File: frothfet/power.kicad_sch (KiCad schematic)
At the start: 41 parts, among them J1 Screw_Terminal_01x08, J2 Screw_Terminal_01x08, U27 TPS7A2033PDBVR, U28 MCP3425A0T-ECH, U30 XL1509-5.0

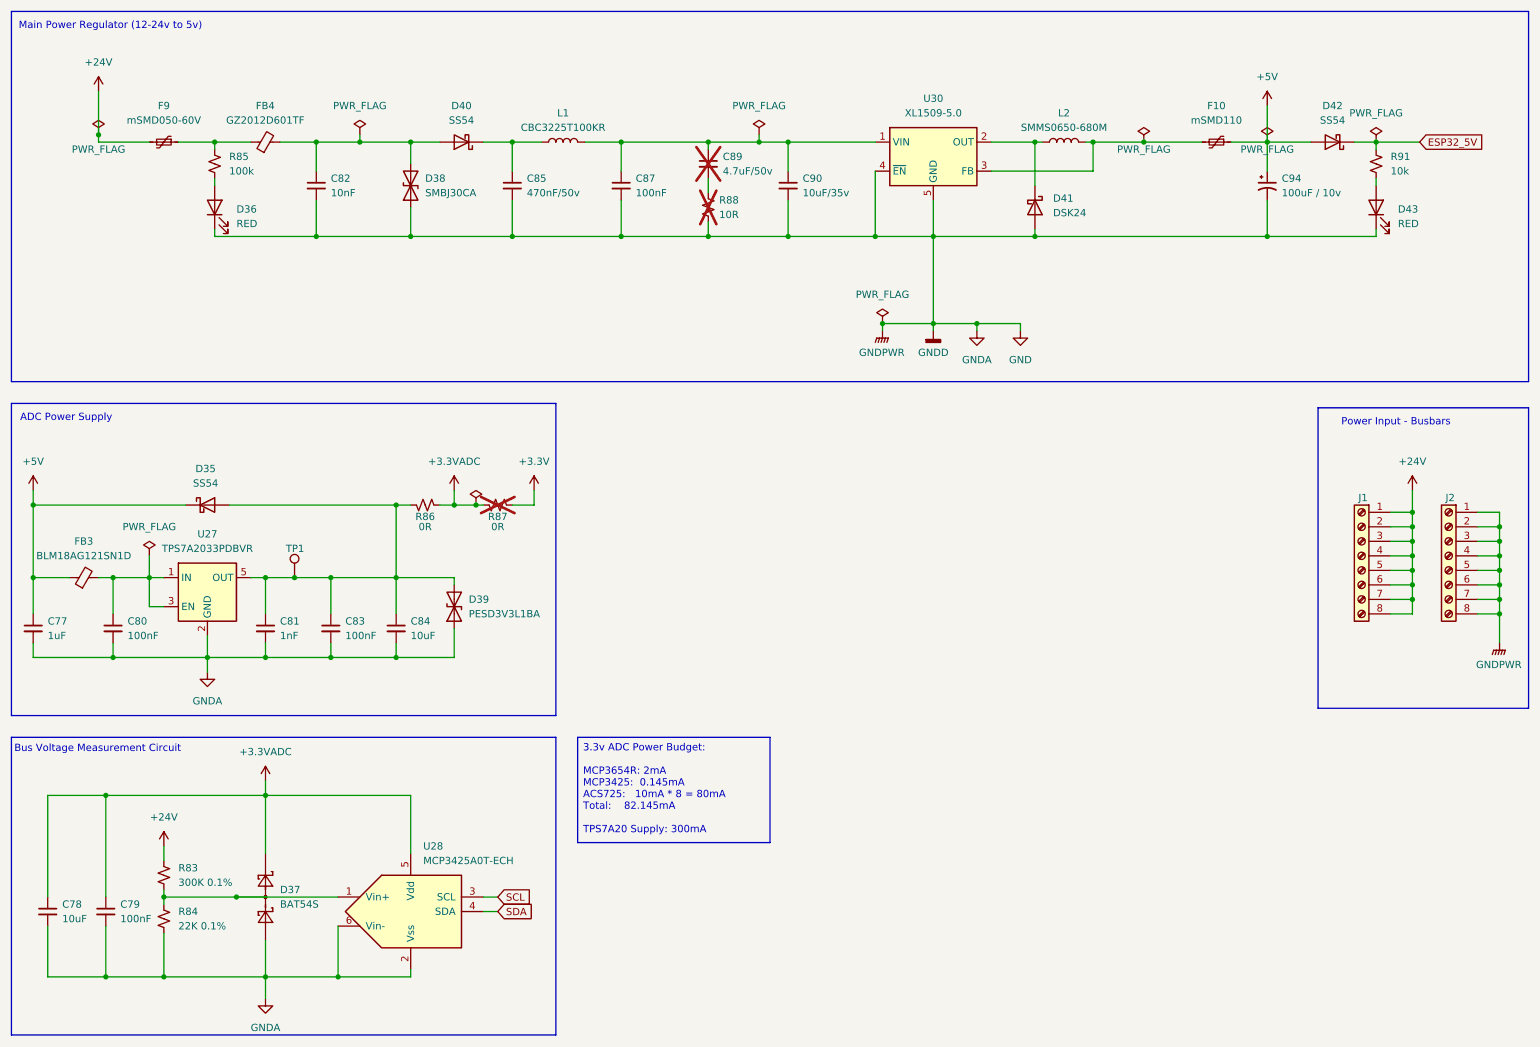
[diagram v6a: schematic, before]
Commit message: wired the i2c addresses.
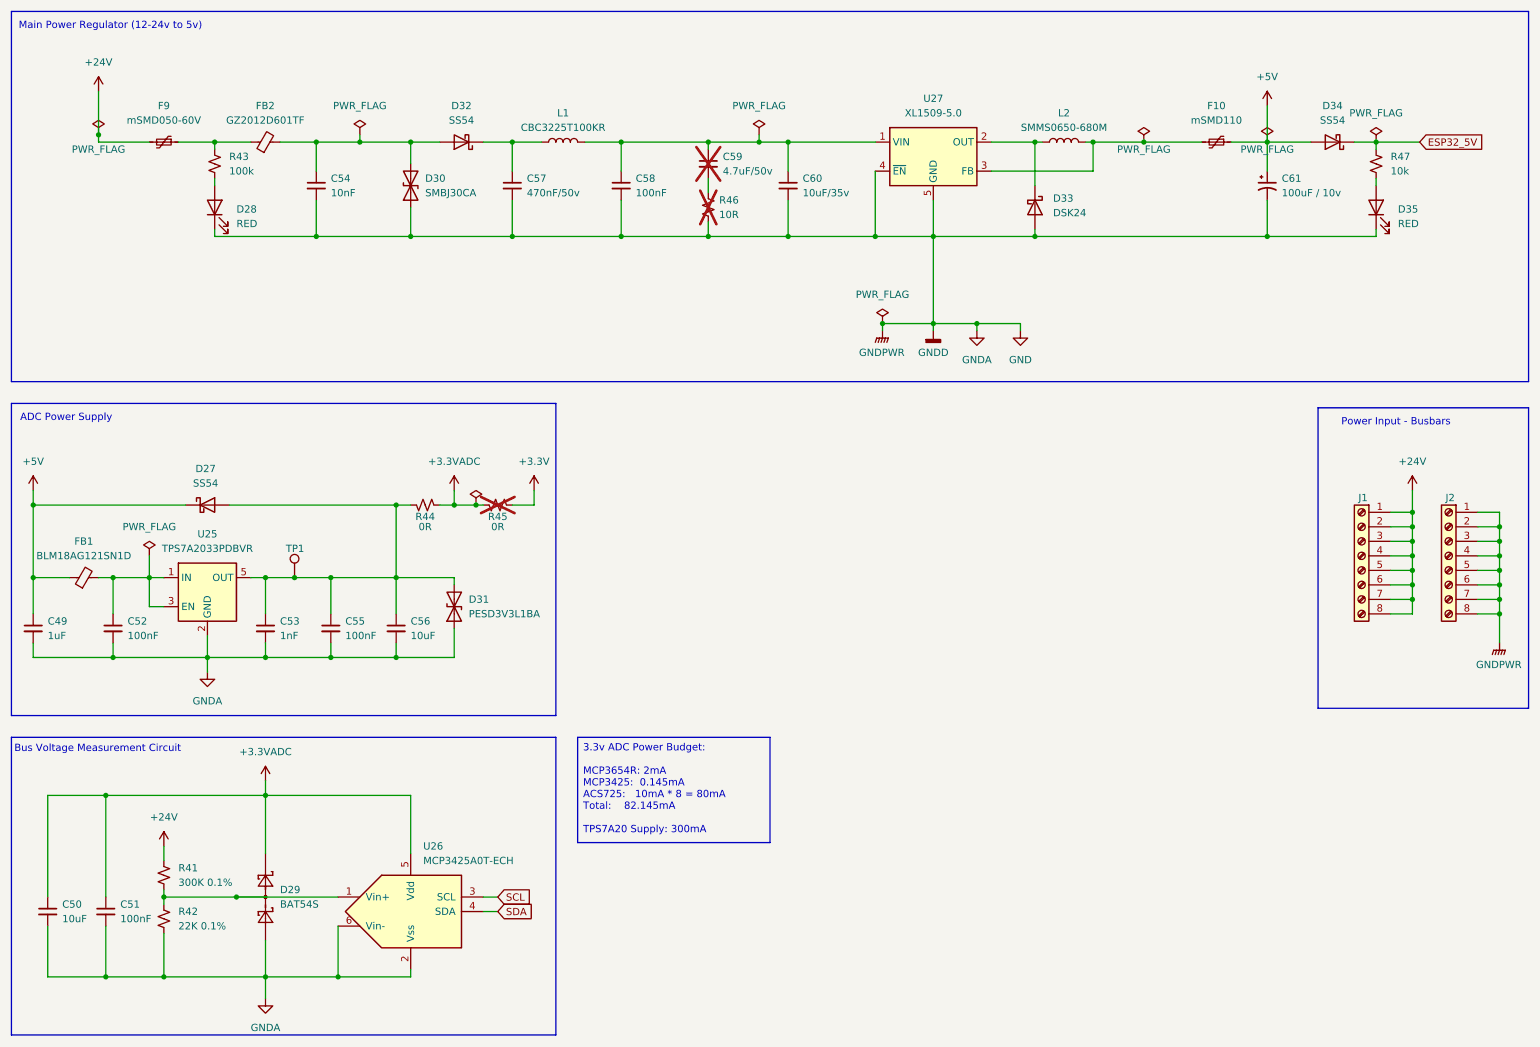
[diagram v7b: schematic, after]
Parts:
- renumbered C77 to C49, C78 to C50, C79 to C51, C80 to C52, C81 to C53, C82 to C54, C83 to C55, C84 to C56, C85 to C57, C87 to C58, C89 to C59, C90 to C60, C94 to C61, D35 to D27, D36 to D28, D37 to D29, D38 to D30, D39 to D31, D40 to D32, D41 to D33, D42 to D34, D43 to D35, FB3 to FB1, FB4 to FB2, R83 to R41, R84 to R42, R85 to R43, R86 to R44, R87 to R45, R88 to R46, R91 to R47, U27 to U25, U28 to U26, U30 to U27

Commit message: added the buffer circuit
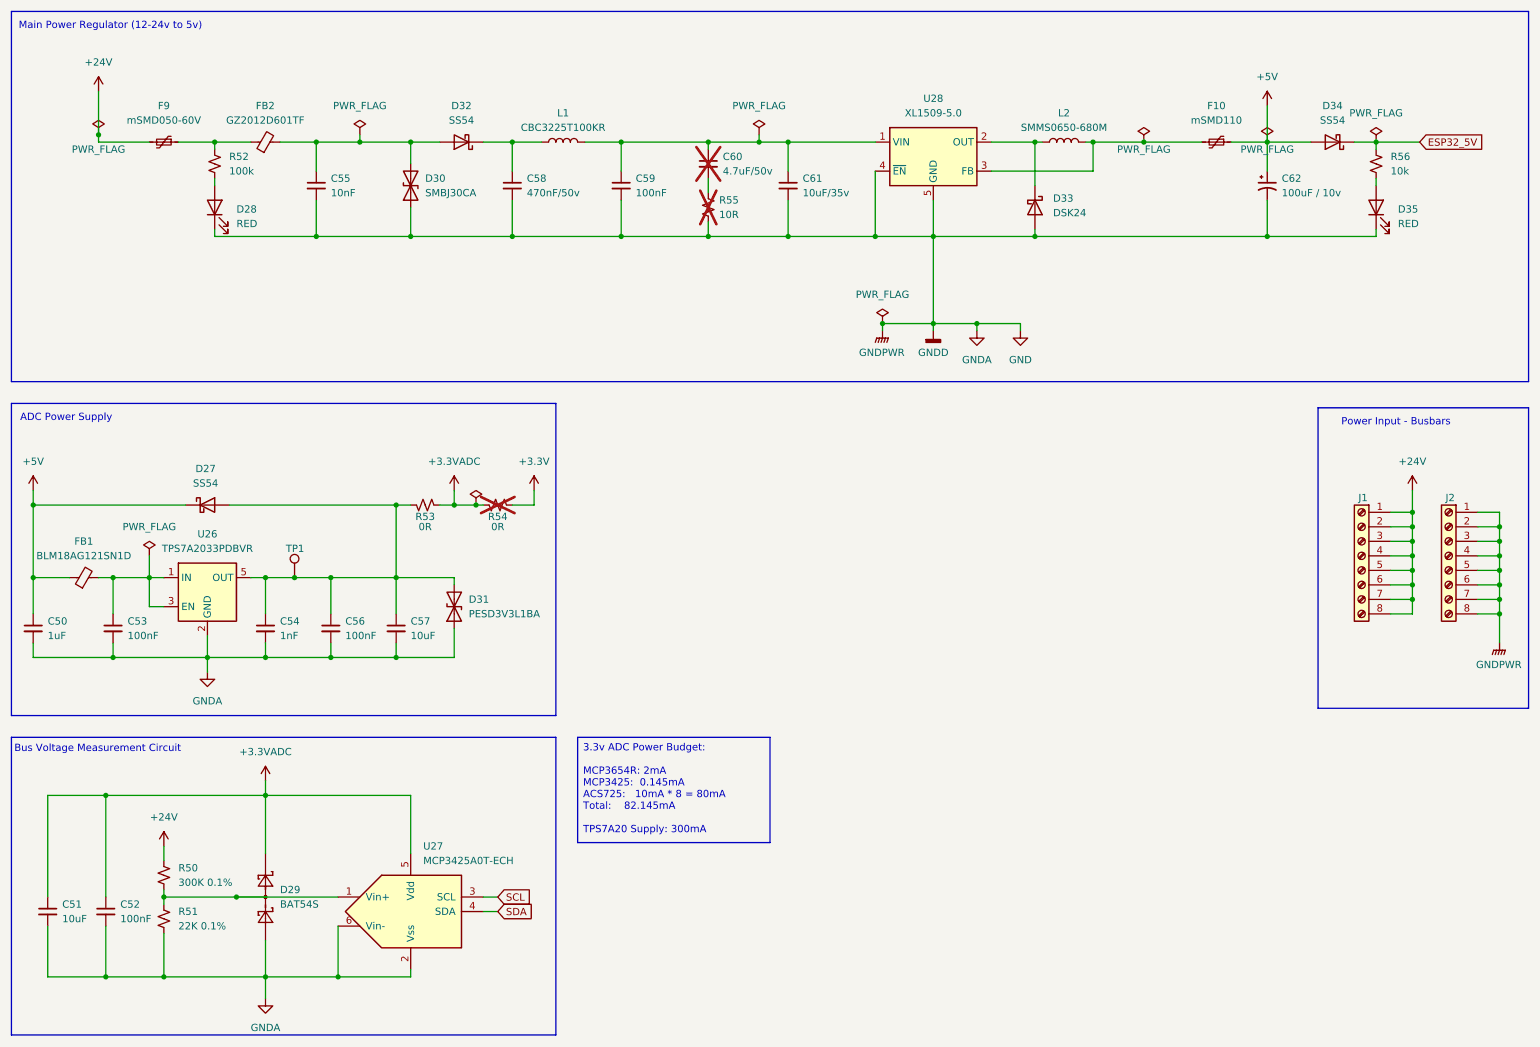
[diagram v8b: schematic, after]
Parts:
- renumbered C49 to C50, C50 to C51, C51 to C52, C52 to C53, C53 to C54, C54 to C55, C55 to C56, C56 to C57, C57 to C58, C58 to C59, C59 to C60, C60 to C61, C61 to C62, R41 to R50, R42 to R51, R43 to R52, R44 to R53, R45 to R54, R46 to R55, R47 to R56, U25 to U26, U26 to U27, U27 to U28
